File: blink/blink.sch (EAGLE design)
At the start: 11 parts, among them T1 2N3904, T2 2N3904

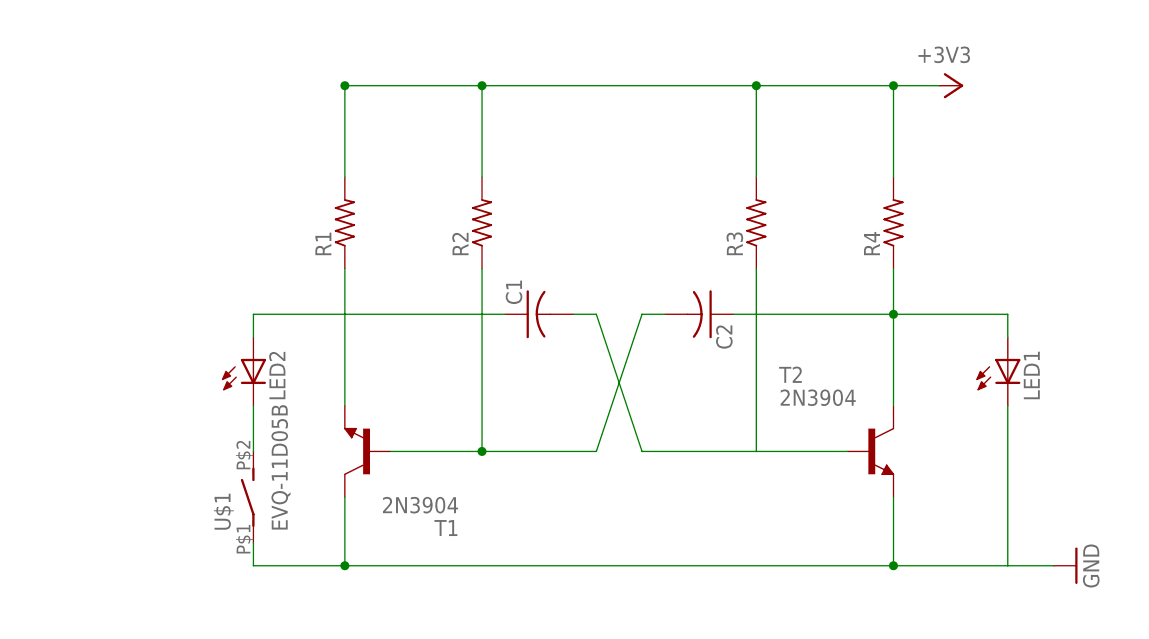
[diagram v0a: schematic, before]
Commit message: modified blink board
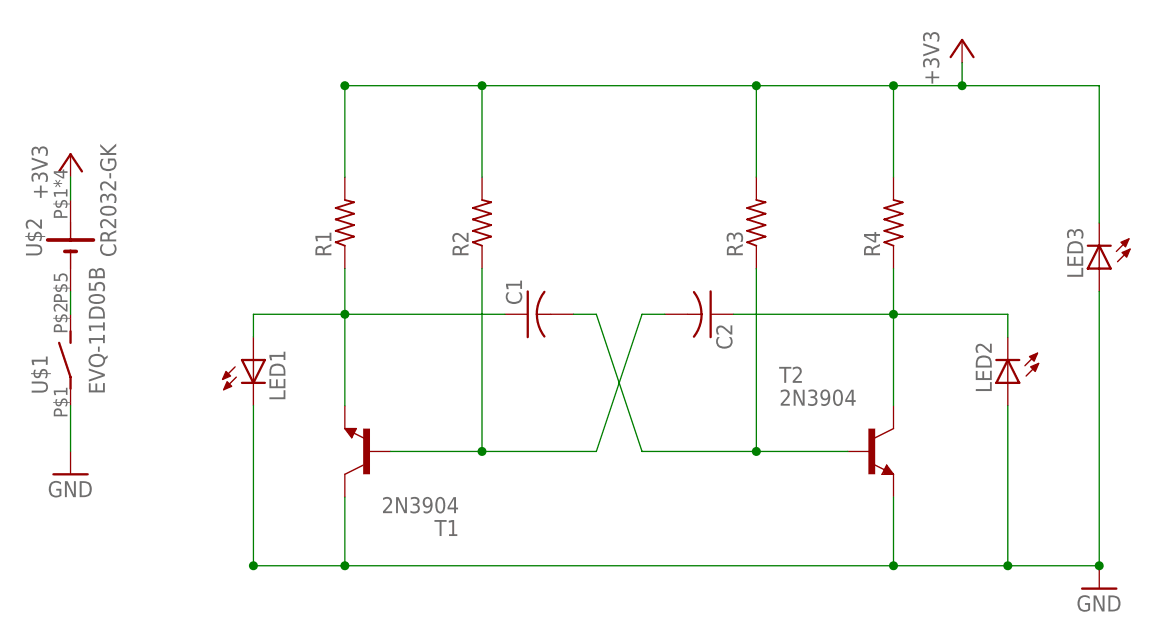
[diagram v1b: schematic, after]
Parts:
- added LED3: (no value), led:LED5MM
- added U$2: CR2032-GK, battery:CR2032-GK
- LED1, LED2: device led:LED5MM -> led:LED3MM
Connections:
- new net N$4: C1.2, R3.1, T2.B
- new net N$5: C2.2, R2.1, T1.B
- net +3V3: now also LED3.C, U$2.+
- net GND: now also LED2.A, LED3.A
- net N$1: now also LED1.A; no longer C2.2, LED2.A, R2.1, T1.B
- net N$2: now also U$2.-; no longer LED2.C
- net N$3: now also LED2.C; no longer C1.2, LED1.A, R3.1, T2.B
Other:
- moved on the sheet: LED1, LED2, U$1
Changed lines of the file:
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@@
 <part name="C1" library="resistor" deviceset="C-US" device="025-030X050"/>
 <part name="C2" library="resistor" deviceset="C-US" device="025-030X050"/>
-<part name="LED1" library="led" deviceset="LED" device="5MM"/>
-<part name="LED2" library="led" deviceset="LED" device="5MM"/>
 <part name="+3V1" library="supply1" deviceset="+3V3" device=""/>
 <part name="GND1" library="supply1" deviceset="GND" device=""/>
 <part name="T2" library="transistor" deviceset="2N3904" device=""/>
 <part name="U$1" library="switch" deviceset="EVQ-11D05B" device=""/>
+<part name="LED1" library="led" deviceset="LED" device="3MM"/>
+<part name="LED2" library="led" deviceset="LED" device="3MM"/>
+<part name="LED3" library="led" deviceset="LED" device="5MM"/>
+<part name="U$2" library="battery" deviceset="CR2032-GK" device=""/>
+<part name="+3V2" library="supply1" deviceset="+3V3" device=""/>
+<part name="GND2" library="supply1" deviceset="GND" device=""/>
 </parts>
 <sheets>
@@
 <instance part="C1" gate="G$1" x="30.48" y="66.04" rot="R90"/>
 <instance part="C2" gate="G$1" x="50.8" y="66.04" rot="R270"/>
-<instance part="LED1" gate="G$1" x="83.82" y="60.96"/>
-<instance part="LED2" gate="G$1" x="0" y="60.96"/>
-<instance part="+3V1" gate="G$1" x="78.74" y="91.44" rot="R270"/>
-<instance part="GND1" gate="1" x="91.44" y="38.1" rot="R90"/>
+<instance part="+3V1" gate="G$1" x="78.74" y="96.52"/>
+<instance part="GND1" gate="1" x="93.98" y="35.56"/>
 <instance part="T2" gate="G1" x="68.58" y="50.8"/>
-<instance part="U$1" gate="G$1" x="0" y="45.72"/>
+<instance part="U$1" gate="G$1" x="-20.32" y="60.96"/>
+<instance part="LED1" gate="G$1" x="0" y="60.96"/>
+<instance part="LED2" gate="G$1" x="83.82" y="58.42" rot="R180"/>
+<instance part="LED3" gate="G$1" x="93.98" y="71.12" rot="R180"/>
+<instance part="U$2" gate="G$1" x="-20.32" y="73.66" rot="R90"/>
+<instance part="+3V2" gate="G$1" x="-20.32" y="83.82"/>
+<instance part="GND2" gate="1" x="-20.32" y="48.26"/>
 </instances>
 <busses>
@@
 <segment>
 <pinref part="+3V1" gate="G$1" pin="+3V3"/>
-<wire x1="76.2" y1="91.44" x2="71.12" y2="91.44" width="0.1524" layer="91"/>
+<wire x1="78.74" y1="93.98" x2="78.74" y2="91.44" width="0.1524" layer="91"/>
+<wire x1="78.74" y1="91.44" x2="71.12" y2="91.44" width="0.1524" layer="91"/>
 <pinref part="R1" gate="G$1" pin="2"/>
 <wire x1="71.12" y1="91.44" x2="55.88" y2="91.44" width="0.1524" layer="91"/>
@@
 <junction x="10.16" y="91.44"/>
 <pinref part="R2" gate="G$1" pin="2"/>
+<pinref part="LED3" gate="G$1" pin="C"/>
+<wire x1="93.98" y1="76.2" x2="93.98" y2="91.44" width="0.1524" layer="91"/>
+<wire x1="93.98" y1="91.44" x2="78.74" y2="91.44" width="0.1524" layer="91"/>
+<junction x="78.74" y="91.44"/>
+</segment>
+<segment>
+<pinref part="U$2" gate="G$1" pin="+"/>
+<pinref part="+3V2" gate="G$1" pin="+3V3"/>
+<wire x1="-20.32" y1="78.74" x2="-20.32" y2="81.28" width="0.1524" layer="91"/>
 </segment>
 </net>
@@
 <pinref part="R1" gate="G$1" pin="1"/>
 <wire x1="10.16" y1="71.12" x2="10.16" y2="66.04" width="0.1524" layer="91"/>
-<wire x1="10.16" y1="66.04" x2="25.4" y2="66.04" width="0.1524" layer="91"/>
-<pinref part="R2" gate="G$1" pin="1"/>
-<wire x1="25.4" y1="66.04" x2="25.4" y2="71.12" width="0.1524" layer="91"/>
+<wire x1="10.16" y1="66.04" x2="27.94" y2="66.04" width="0.1524" layer="91"/>
 <pinref part="T1" gate="G1" pin="E"/>
 <wire x1="10.16" y1="66.04" x2="10.16" y2="55.88" width="0.1524" layer="91"/>
-<pinref part="LED2" gate="G$1" pin="A"/>
 <wire x1="10.16" y1="66.04" x2="0" y2="66.04" width="0.1524" layer="91"/>
 <wire x1="0" y1="66.04" x2="0" y2="63.5" width="0.1524" layer="91"/>
-<wire x1="25.4" y1="66.04" x2="25.4" y2="50.8" width="0.1524" layer="91"/>
-<pinref part="T1" gate="G1" pin="B"/>
-<wire x1="25.4" y1="50.8" x2="15.24" y2="50.8" width="0.1524" layer="91"/>
 <pinref part="C1" gate="G$1" pin="1"/>
-<wire x1="25.4" y1="66.04" x2="27.94" y2="66.04" width="0.1524" layer="91"/>
-<pinref part="C2" gate="G$1" pin="2"/>
-<wire x1="45.72" y1="66.04" x2="43.18" y2="66.04" width="0.1524" layer="91"/>
-<wire x1="43.18" y1="66.04" x2="38.1" y2="50.8" width="0.1524" layer="91"/>
-<wire x1="38.1" y1="50.8" x2="25.4" y2="50.8" width="0.1524" layer="91"/>
-<junction x="25.4" y="50.8"/>
+<pinref part="LED1" gate="G$1" pin="A"/>
+<junction x="10.16" y="66.04"/>
 </segment>
 </net>
@@
 <wire x1="10.16" y1="38.1" x2="71.12" y2="38.1" width="0.1524" layer="91"/>
 <wire x1="71.12" y1="38.1" x2="83.82" y2="38.1" width="0.1524" layer="91"/>
-<wire x1="83.82" y1="38.1" x2="88.9" y2="38.1" width="0.1524" layer="91"/>
+<wire x1="83.82" y1="38.1" x2="93.98" y2="38.1" width="0.1524" layer="91"/>
 <wire x1="10.16" y1="45.72" x2="10.16" y2="38.1" width="0.1524" layer="91"/>
-<pinref part="LED1" gate="G$1" pin="C"/>
 <wire x1="83.82" y1="55.88" x2="83.82" y2="38.1" width="0.1524" layer="91"/>
 <pinref part="T2" gate="G1" pin="E"/>
@@
 <junction x="71.12" y="38.1"/>
 <junction x="10.16" y="38.1"/>
+<pinref part="LED2" gate="G$1" pin="A"/>
+<pinref part="LED3" gate="G$1" pin="A"/>
+<wire x1="93.98" y1="38.1" x2="93.98" y2="68.58" width="0.1524" layer="91"/>
+<junction x="93.98" y="38.1"/>
+<junction x="83.82" y="38.1"/>
+<pinref part="LED1" gate="G$1" pin="C"/>
+<wire x1="0" y1="38.1" x2="0" y2="55.88" width="0.1524" layer="91"/>
+<junction x="0" y="38.1"/>
+</segment>
+<segment>
+<pinref part="GND2" gate="1" pin="GND"/>
 <pinref part="U$1" gate="G$1" pin="P"/>
-<wire x1="0" y1="38.1" x2="0" y2="40.64" width="0.1524" layer="91"/>
+<wire x1="-20.32" y1="50.8" x2="-20.32" y2="55.88" width="0.1524" layer="91"/>
 </segment>
 </net>
 <net name="N$3" class="0">
 <segment>
-<pinref part="R3" gate="G$1" pin="1"/>
-<wire x1="55.88" y1="71.12" x2="55.88" y2="66.04" width="0.1524" layer="91"/>
 <pinref part="C2" gate="G$1" pin="1"/>
-<wire x1="55.88" y1="66.04" x2="53.34" y2="66.04" width="0.1524" layer="91"/>
 <pinref part="R4" gate="G$1" pin="1"/>
 <wire x1="71.12" y1="71.12" x2="71.12" y2="66.04" width="0.1524" layer="91"/>
-<wire x1="71.12" y1="66.04" x2="55.88" y2="66.04" width="0.1524" layer="91"/>
+<wire x1="71.12" y1="66.04" x2="53.34" y2="66.04" width="0.1524" layer="91"/>
 <wire x1="71.12" y1="66.04" x2="83.82" y2="66.04" width="0.1524" layer="91"/>
-<pinref part="LED1" gate="G$1" pin="A"/>
 <wire x1="83.82" y1="66.04" x2="83.82" y2="63.5" width="0.1524" layer="91"/>
 <pinref part="T2" gate="G1" pin="C"/>
 <wire x1="71.12" y1="66.04" x2="71.12" y2="55.88" width="0.1524" layer="91"/>
+<junction x="71.12" y="66.04"/>
+<pinref part="LED2" gate="G$1" pin="C"/>
+</segment>
+</net>
+<net name="N$4" class="0">
+<segment>
+<pinref part="T2" gate="G1" pin="B"/>
 <pinref part="C1" gate="G$1" pin="2"/>
 <wire x1="35.56" y1="66.04" x2="38.1" y2="66.04" width="0.1524" layer="91"/>
 <wire x1="38.1" y1="66.04" x2="43.18" y2="50.8" width="0.1524" layer="91"/>
 <wire x1="43.18" y1="50.8" x2="55.88" y2="50.8" width="0.1524" layer="91"/>
-<wire x1="55.88" y1="50.8" x2="55.88" y2="66.04" width="0.1524" layer="91"/>
-<junction x="71.12" y="66.04"/>
-<pinref part="T2" gate="G1" pin="B"/>
+<pinref part="R3" gate="G$1" pin="1"/>
 <wire x1="55.88" y1="50.8" x2="66.04" y2="50.8" width="0.1524" layer="91"/>
+<wire x1="55.88" y1="71.12" x2="55.88" y2="50.8" width="0.1524" layer="91"/>
+<junction x="55.88" y="50.8"/>
+</segment>
+</net>
+<net name="N$5" class="0">
+<segment>
+<pinref part="T1" gate="G1" pin="B"/>
+<pinref part="C2" gate="G$1" pin="2"/>
+<wire x1="45.72" y1="66.04" x2="43.18" y2="66.04" width="0.1524" layer="91"/>
+<wire x1="43.18" y1="66.04" x2="38.1" y2="50.8" width="0.1524" layer="91"/>
+<wire x1="38.1" y1="50.8" x2="25.4" y2="50.8" width="0.1524" layer="91"/>
+<pinref part="R2" gate="G$1" pin="1"/>
+<wire x1="25.4" y1="50.8" x2="15.24" y2="50.8" width="0.1524" layer="91"/>
+<wire x1="25.4" y1="71.12" x2="25.4" y2="50.8" width="0.1524" layer="91"/>
+<junction x="25.4" y="50.8"/>
 </segment>
 </net>
@@
 <segment>
 <pinref part="U$1" gate="G$1" pin="S"/>
-<pinref part="LED2" gate="G$1" pin="C"/>
-<wire x1="0" y1="50.8" x2="0" y2="55.88" width="0.1524" layer="91"/>
+<pinref part="U$2" gate="G$1" pin="-"/>
+<wire x1="-20.32" y1="66.04" x2="-20.32" y2="68.58" width="0.1524" layer="91"/>
 </segment>
 </net>
